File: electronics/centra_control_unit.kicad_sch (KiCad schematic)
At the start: 40 parts, among them J1 GND NetTie, J10 water_sensor_conn, J2 CAN, J3 Conn 12V Out 5ch, Q2 IRF6802SD, Q3 IRF6802SD, U1 AZ1117-ADJ, U10 BTS7006, U2 AZ1117-ADJ, U3 TJA1051T-3, U4 ESP32-S3-MINI-1U, U5 CD74HC4067SM, U6 BTS7006, U7 BTS7006, U8 BTS7006, U9 BTS7006

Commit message: porady od MichalaG
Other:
- added sheet water_sensors_logic (water_sensors_logic.kicad_sch)
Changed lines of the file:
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@@
 		)
 		(instances
-			(project ""
+			(project "electronics"
 				(path "/eeb1234c-eae0-4ac6-a30d-2a978d66d889/04c402f1-b99a-4823-99a0-0c7312782f29"
 					(reference "R1")
@@
 		)
 		(instances
-			(project ""
+			(project "electronics"
 				(path "/eeb1234c-eae0-4ac6-a30d-2a978d66d889/04c402f1-b99a-4823-99a0-0c7312782f29"
 					(reference "#PWR05")
@@
 		)
 		(instances
-			(project ""
+			(project "electronics"
 				(path "/eeb1234c-eae0-4ac6-a30d-2a978d66d889/04c402f1-b99a-4823-99a0-0c7312782f29"
 					(reference "Q2")
@@
 		)
 		(instances
-			(project ""
+			(project "electronics"
 				(path "/eeb1234c-eae0-4ac6-a30d-2a978d66d889/04c402f1-b99a-4823-99a0-0c7312782f29"
 					(reference "J1")
@@
 		)
 		(instances
-			(project ""
+			(project "electronics"
 				(path "/eeb1234c-eae0-4ac6-a30d-2a978d66d889/04c402f1-b99a-4823-99a0-0c7312782f29"
 					(reference "#PWR011")
@@
 		)
 		(instances
-			(project ""
+			(project "electronics"
 				(path "/eeb1234c-eae0-4ac6-a30d-2a978d66d889/04c402f1-b99a-4823-99a0-0c7312782f29"
 					(reference "#PWR018")
@@
 		)
 		(instances
-			(project ""
+			(project "electronics"
 				(path "/eeb1234c-eae0-4ac6-a30d-2a978d66d889/04c402f1-b99a-4823-99a0-0c7312782f29"
 					(reference "U3")
@@
 		)
 		(instances
-			(project ""
+			(project "electronics"
 				(path "/eeb1234c-eae0-4ac6-a30d-2a978d66d889/04c402f1-b99a-4823-99a0-0c7312782f29"
 					(reference "C2")
@@
 		)
 		(instances
-			(project ""
+			(project "electronics"
 				(path "/eeb1234c-eae0-4ac6-a30d-2a978d66d889/04c402f1-b99a-4823-99a0-0c7312782f29"
 					(reference "U4")
@@
 		)
 		(instances
-			(project ""
+			(project "electronics"
 				(path "/eeb1234c-eae0-4ac6-a30d-2a978d66d889/04c402f1-b99a-4823-99a0-0c7312782f29"
 					(reference "#PWR017")
@@
 		)
 		(instances
-			(project ""
+			(project "electronics"
 				(path "/eeb1234c-eae0-4ac6-a30d-2a978d66d889/04c402f1-b99a-4823-99a0-0c7312782f29"
 					(reference "U1")
@@
 		)
 		(instances
-			(project ""
+			(project "electronics"
 				(path "/eeb1234c-eae0-4ac6-a30d-2a978d66d889/04c402f1-b99a-4823-99a0-0c7312782f29"
 					(reference "Q2")
@@
 				)
 			)
+		)
+	)
+	(sheet
+		(at 151.13 19.05)
+		(size 21.59 13.97)
+		(fields_autoplaced yes)
+		(stroke
+			(width 0.1524)
+			(type solid)
+		)
+		(fill
+			(color 0 0 0 0.0000)
+		)
+		(property "Sheetname" "water_sensors_logic"
+			(at 151.13 18.3384 0)
+			(effects
+				(font
+					(size 1.27 1.27)
+				)
+				(justify left bottom)
+			)
+		)
+		(property "Sheetfile" "water_sensors_logic.kicad_sch"
+			(at 151.13 33.6046 0)
+			(effects
+				(font
+					(size 1.27 1.27)
+				)
+				(justify left top)
+			)
+		)
+		(instances
+			(project "electronics"
+				(path "/eeb1234c-eae0-4ac6-a30d-2a978d66d889/04c402f1-b99a-4823-99a0-0c7312782f29"
+					(page "6")
+				)
+			)

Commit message: lisbon flight changes
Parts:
- removed J10: water_sensor_conn, TerminalBlock:TerminalBlock_Xinya_XY308-2.54-6P_1x06_P2.54mm_Horizontal, symbol Connector_Generic:Conn_01x06
- removed J3: Conn 12V Out 5ch, TerminalBlock:TerminalBlock_bornier-5_P5.08mm, symbol Connector_Generic:Conn_01x05
- removed U5: CD74HC4067SM, Package_SO:SSOP-24_5.3x8.2mm_P0.65mm, symbol 74xx:CD74HC4067SM
- added J13: CH2, symbol Connector_Generic:Conn_01x01
- added J14: CH3, symbol Connector_Generic:Conn_01x01
- added J15: CH4, symbol Connector_Generic:Conn_01x01
- added J16: CH5, symbol Connector_Generic:Conn_01x01
- added J3: CH1, symbol Connector_Generic:Conn_01x01
- added U13: TMUX1108PW, Package_SO:TSSOP-16_4.4x5mm_P0.65mm, symbol Analog_Switch:TMUX1108PW
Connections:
- net +3.3V: now also U13.3 (VSS)
- net CH1_DIAG: now also U13.4 (S1)
- net CH2_DIAG: now also U13.5 (S2)
- net CH3_DIAG: now also U13.6 (S3)
- net CH4_DIAG: now also U13.7 (S4)
- net CH5_DIAG: now also U13.12 (S5)
- net HP_GND: no longer C_GND1.2, C_GND2.2, C_GND3.2, C_GND4.2, C_GND5.2, U10.1 (GND), U6.1 (GND), U7.1 (GND), U8.1 (GND), U9.1 (GND)
- net MUX_ANALOG_COM: now also U13.8 (D)
- net MUX_S0: now also U13.1 (A0)
- net MUX_S1: now also U13.16 (A1)
- net MUX_S2: now also U13.15 (A2)
- net at C_GND1.1, U6.10 (OUT), U6.12 (OUT)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: now also J3.1 (Pin_1)
- net at C_GND2.1, U7.10 (OUT), U7.12 (OUT)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: now also J13.1 (Pin_1)
- net at C_GND3.1, U8.10 (OUT), U8.12 (OUT)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: now also J14.1 (Pin_1)
- net at C_GND4.1, U9.10 (OUT), U9.12 (OUT)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: now also J15.1 (Pin_1)
- net at C_GND5.1, U10.10 (OUT), U10.12 (OUT)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: now also J16.1 (Pin_1)
- new net GND_HP: C_GND1.2, C_GND2.2, C_GND3.2, C_GND4.2, C_GND5.2, U10.1 (GND), U6.1 (GND), U7.1 (GND), U8.1 (GND), U9.1 (GND)
- new net GND_LP: U13.14 (GND)
- no-connect marks 19 -> 13

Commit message: flight back. different layout. start analog ui
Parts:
- removed C1, C2: 10uF, Capacitor_SMD:C_0805_2012Metric_Pad1.18x1.45mm_HandSolder, symbol Device:C
- removed C3, C4: 22uF, Capacitor_SMD:C_0805_2012Metric_Pad1.18x1.45mm_HandSolder, symbol Device:C
- removed C_GND1, C_GND2, C_GND3, C_GND4, C_GND5: 10nF, Capacitor_SMD:C_0805_2012Metric_Pad1.18x1.45mm_HandSolder, symbol Device:C_Small
- removed J1: GND NetTie, Connector_PinHeader_1.00mm:PinHeader_1x02_P1.00mm_Vertical, symbol Connector_Generic:Conn_01x02
- removed J13: CH2, symbol Connector_Generic:Conn_01x01
- removed J14: CH3, symbol Connector_Generic:Conn_01x01
- removed J15: CH4, symbol Connector_Generic:Conn_01x01
- removed J16: CH5, symbol Connector_Generic:Conn_01x01
- removed J2: CAN, TerminalBlock:TerminalBlock_Xinya_XY308-2.54-2P_1x02_P2.54mm_Horizontal, symbol Connector_Generic:Conn_01x02
- removed J3: CH1, symbol Connector_Generic:Conn_01x01
- removed Q2, Q3: IRF6802SD, Package_DirectFET:DirectFET_SA, symbol Transistor_FET:IRF6802SD
- removed R1, R3: 125, Resistor_SMD:R_0805_2012Metric_Pad1.20x1.40mm_HandSolder, symbol Device:R
- removed R2: 205, Resistor_SMD:R_0805_2012Metric_Pad1.20x1.40mm_HandSolder, symbol Device:R
- removed R4: 370, Resistor_SMD:R_0805_2012Metric_Pad1.20x1.40mm_HandSolder, symbol Device:R
- removed R_DEN1, R_DEN2, R_DEN3, R_DEN4, R_DEN5, R_IN1, R_IN2, R_IN3, R_IN4, R_IN5: 4.7k, Resistor_SMD:R_0805_2012Metric_Pad1.20x1.40mm_HandSolder, symbol Device:R
- removed U1, U2: AZ1117-ADJ, Package_TO_SOT_SMD:SOT-223-3_TabPin2, symbol Regulator_Linear:AZ1117-ADJ
- removed U10, U6, U7, U8, U9: BTS7006, Package_SO:Infineon_PG-TSDSO-14-22, symbol Power_Management:BTS7004-1EPP
- removed U13: TMUX1108PW, Package_SO:TSSOP-16_4.4x5mm_P0.65mm, symbol Analog_Switch:TMUX1108PW
- removed U3: TJA1051T-3, Package_SO:SOIC-8_3.9x4.9mm_P1.27mm, symbol Interface_CAN_LIN:TJA1051T-3
- added FB2: FerriteBead 47 Ohm, Inductor_SMD:L_Walsin_WLFM201609x, symbol Device:FerriteBead
- added U14: CD74HC4067SM, Package_SO:SSOP-24_5.3x8.2mm_P0.65mm, symbol 74xx:CD74HC4067SM
- added U15: TCA9555PWR, Package_SO:TSSOP-24_4.4x7.8mm_P0.65mm, symbol Interface_Expansion:TCA9555PWR
- added U18: SN74LV4051A, symbol 74xx:74LS151
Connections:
- net GND is gone; now on net GND_LP: U4.1 (GND), U4.2 (GND), U4.42 (GND), U4.43 (GND), U4.46 (GND), U4.47 (GND), U4.48 (GND), U4.49 (GND), U4.50 (GND), U4.51 (GND), U4.52 (GND), U4.53 (GND), U4.54 (GND), U4.55 (GND), U4.56 (GND), U4.57 (GND), U4.58 (GND), U4.59 (GND), U4.60 (GND), U4.61 (GND), U4.62 (GND), U4.63 (GND), U4.64 (GND), U4.65 (GND)
- net GND_HP: now also FB2.2
- net GND_LP: now also FB2.1, U15.12 (GND), U15.2 (A1), U15.21 (A0), U15.3 (A2)
- net SCL: now also U15.22 (SCL)
- net SDA: now also U15.23 (SDA)
- net CAN_RX: no longer names the net of U4.13 (IO9)
- net CAN_SLEEP: no longer names the net of U4.14 (IO10)
- net CAN_TX: no longer names the net of U4.12 (IO8)
- net CH1_DIAG_EN renamed ch4_diag
- net CH1_IN renamed ch5_diag
- net CH2_DAIG_EN renamed ch2_diag
- net CH2_IN renamed ch3_diag
- net CH3_DAIG_EN: no longer names the net of U4.35 (IO39)
- net CH3_DAIG_EN: now also U15.1 (~{INT})
- net CH3_IN renamed ch1_diag
- net CH4_DAIG_EN: no longer names the net of U4.33 (IO37)
- net CH4_IN: no longer names the net of U4.34 (IO38)
- net CH5_DAIG_EN: no longer names the net of U4.31 (IO35)
- net CH5_IN: no longer names the net of U4.32 (IO36)
- net MUX_ANALOG_COM renamed 230VAC/AC_DETECT
- net MUX_S0 renamed temp_sensors/1-WIRE
- net MUX_S1 renamed CAN/CAN_SLEEP
- net MUX_S2 renamed CAN/CAN_RX
- net MUX_S3 renamed CAN/CAN_TX
- net water_sens_enable renamed 230VAC/RELAY_IN
- new net digital_switching/CH1_DEN: U15.11 (P07)
- new net digital_switching/CH1_IN: U15.10 (P06)
- new net digital_switching/CH2_DEN: U15.14 (P11)
- new net digital_switching/CH2_IN: U15.13 (P10)
- new net digital_switching/CH3_DEN: U15.16 (P13)
- new net digital_switching/CH3_IN: U15.15 (P12)
- new net digital_switching/CH4_DEN: U15.18 (P15)
- new net digital_switching/CH4_IN: U15.17 (P14)
- new net digital_switching/CH5_DEN: U15.20 (P17)
- new net digital_switching/CH5_IN: U15.19 (P16)
- new net water_sensors_logic/GREY_WATER_FULL: U15.9 (P05)
- new net water_sensors_logic/WS_ENABLE: U15.4 (P00)
- new net water_sensors_logic/WS_LVL_100%: U15.8 (P04)
- new net water_sensors_logic/WS_LVL_25%: U15.5 (P01)
- new net water_sensors_logic/WS_LVL_50%: U15.6 (P02)
- new net water_sensors_logic/WS_LVL_75%: U15.7 (P03)
- no-connect marks 13 -> 23
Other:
- added sheet 230VAC (230VAC.kicad_sch)
- added sheet CAN (CAN.kicad_sch)
- added sheet dc_dc_conversion (dc_dc_conversion.kicad_sch)
- added sheet digital_switching (digital_switching.kicad_sch)
- added sheet rgb_led_control (rgb_led_control.kicad_sch)
- added sheet temp_sensors (temp_sensors.kicad_sch)
- sheet water_sensors_logic ports: added GREY_WATER_FULL, WS_ENABLE, WS_LVL_100%, WS_LVL_25%, WS_LVL_50%, WS_LVL_75%; removed none
- note removed: "LED controls"
- note removed: "Vout=Vref*(1+R2/R1) + Iadj*R2"
- moved on the sheet: D1

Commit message: no tracks, but placement looks good
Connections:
- net +3.3V: now also U15.24 (VCC)
- net +BATT renamed V_Bat
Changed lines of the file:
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@@
 	)
 	(no_connect
-		(at 111.76 53.34)
+		(at 115.57 53.34)
 	)
 	(no_connect
@@
 	(wire
 		(pts
-			(xy 113.03 53.34) (xy 115.57 53.34)
-		)
-		(stroke
-			(width 0)
-			(type default)
-		)
-	)
-	(wire
-		(pts
 			(xy 218.44 62.23) (xy 236.22 62.23)
 		)
@@
 		)
 	)
-	(label "V_Bat"
-		(at 30.48 21.59 0)
-		(fields_autoplaced yes)
-		(effects
-			(font
-				(size 1.27 1.27)
-			)
-			(justify left bottom)
-		)
-	)
 	(label "SCL"
 		(at 109.22 71.12 0)
@@
 	)
 	(label "strap pin"
-		(at 113.03 53.34 180)
+		(at 115.57 53.34 180)
 		(fields_autoplaced yes)
 		(effects
@@
 			)
 			(justify left bottom)
+		)
+	)
+	(global_label "V_Bat"
+		(shape passive)
+		(at 26.67 21.59 180)
+		(fields_autoplaced yes)
+		(effects
+			(font
+				(size 1.27 1.27)
+			)
+			(justify right)
+		)
+		(property "Intersheetrefs" "${INTERSHEET_REFS}"
+			(at 19.5952 21.59 0)
+			(effects
+				(font
+					(size 1.27 1.27)
+				)
+				(justify right)
+				(hide yes)
+			)
 		)
 	)
@@
 		(shape passive)
 		(at 107.95 68.58 180)
-		(fields_autoplaced yes)
-		(effects
-			(font
-				(size 1.27 1.27)
-			)
-			(justify right)
-		)
-	)
-	(hierarchical_label "+BATT"
-		(shape input)
-		(at 26.67 21.59 180)
 		(fields_autoplaced yes)
 		(effects
@@
 					(unit 1)
 				)
+			)
+		)
+	)
+	(symbol
+		(lib_id "power:+3.3V")
+		(at 200.66 41.91 0)
+		(unit 1)
+		(exclude_from_sim no)
+		(in_bom yes)
+		(on_board yes)
+		(dnp no)
+		(fields_autoplaced yes)
+		(property "Reference" "#PWR08"
+			(at 200.66 45.72 0)
+			(effects
+				(font
+					(size 1.27 1.27)
+				)
+				(hide yes)
+			)
+		)
+		(property "Value" "+3.3V"
+			(at 200.66 36.83 0)
+			(effects
+				(font
+					(size 1.27 1.27)
+				)
+			)
+		)
+		(property "Footprint" ""
+			(at 200.66 41.91 0)
+			(effects
+				(font
+					(size 1.27 1.27)
+				)
+				(hide yes)
+			)
+		)
+		(property "Datasheet" ""
+			(at 200.66 41.91 0)
+			(effects
+				(font
+					(size 1.27 1.27)
+				)
+				(hide yes)
+			)
+		)
+		(property "Description" "Power symbol creates a global label with name \"+3.3V\""
+			(at 200.66 41.91 0)
+			(effects
+				(font
+					(size 1.27 1.27)
+				)
+				(hide yes)
+			)
+		)
+		(pin "1"
+		)
+		(instances
+			(project "electronics"
+				(path "/eeb1234c-eae0-4ac6-a30d-2a978d66d889/04c402f1-b99a-4823-99a0-0c7312782f29"
+					(reference "#PWR08")
+					(unit 1)
+				)

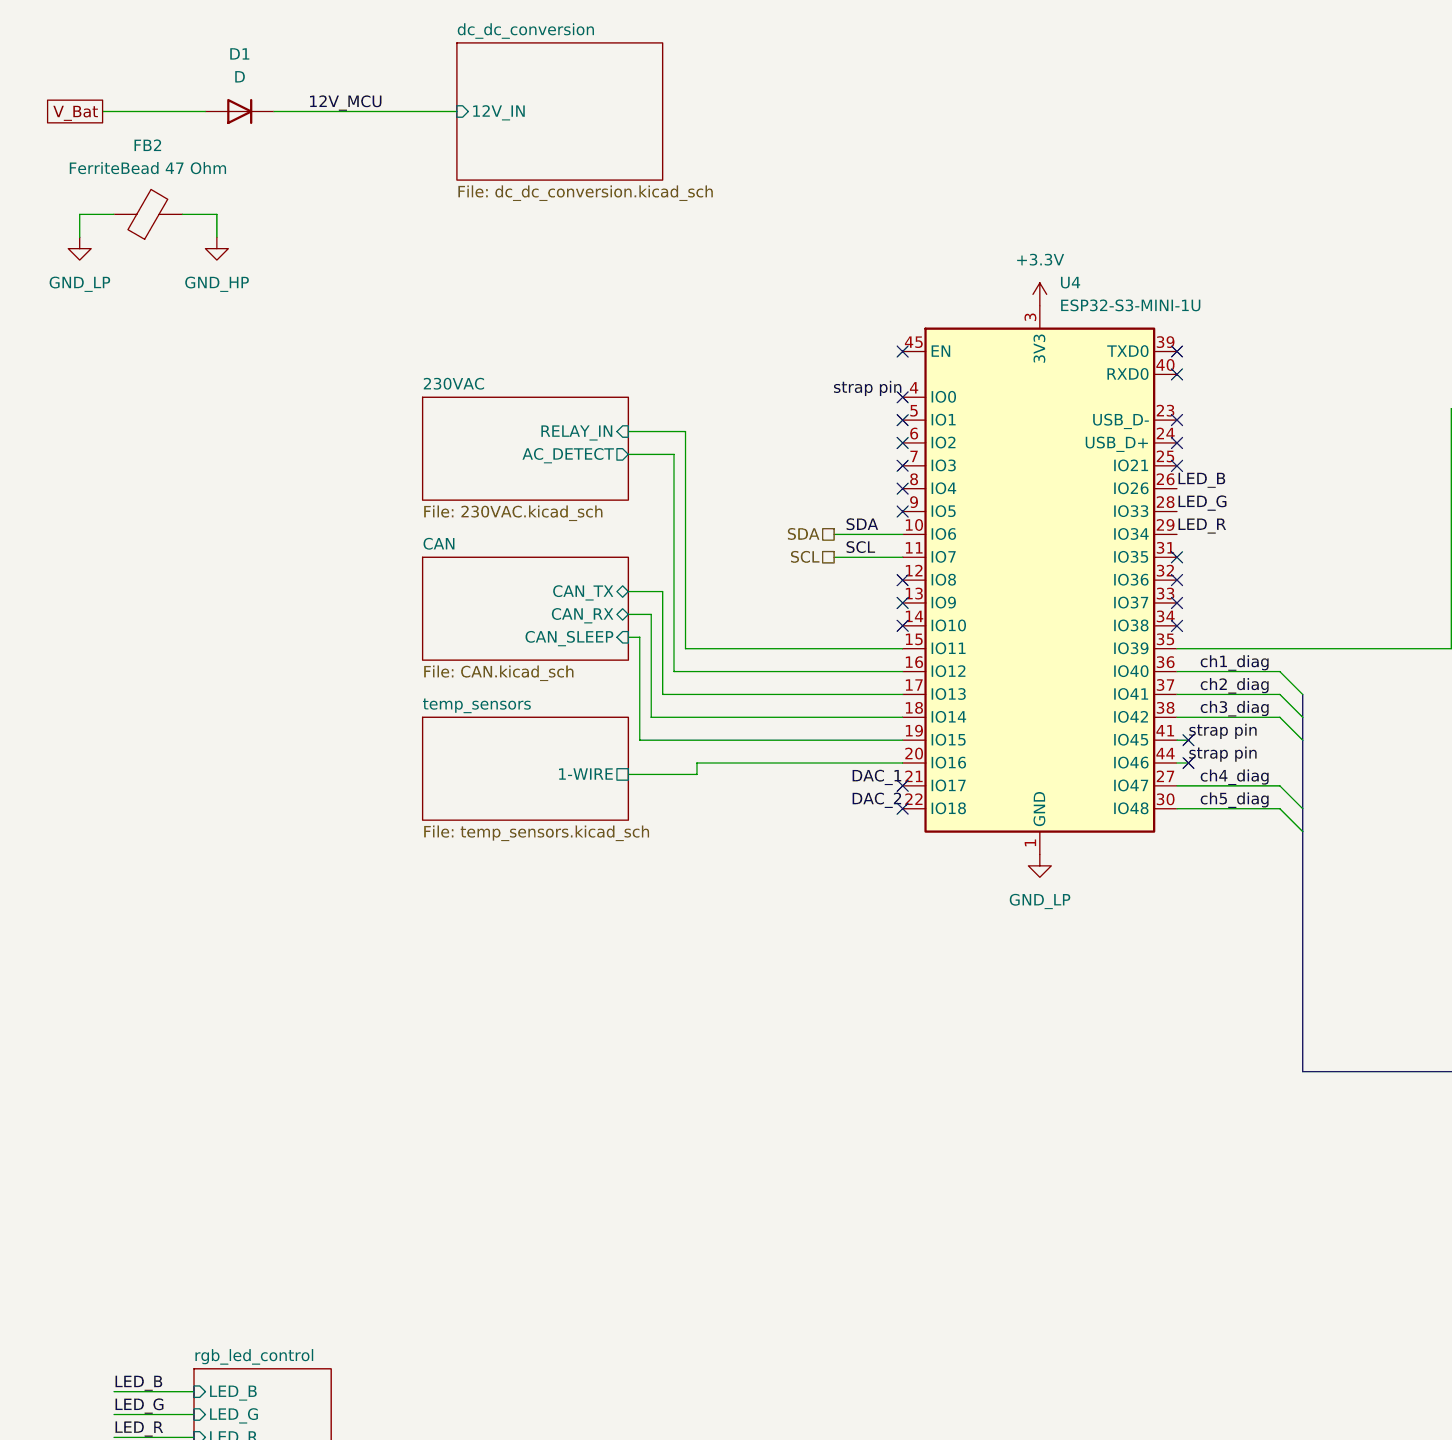
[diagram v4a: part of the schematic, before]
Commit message: add some more part nummbers
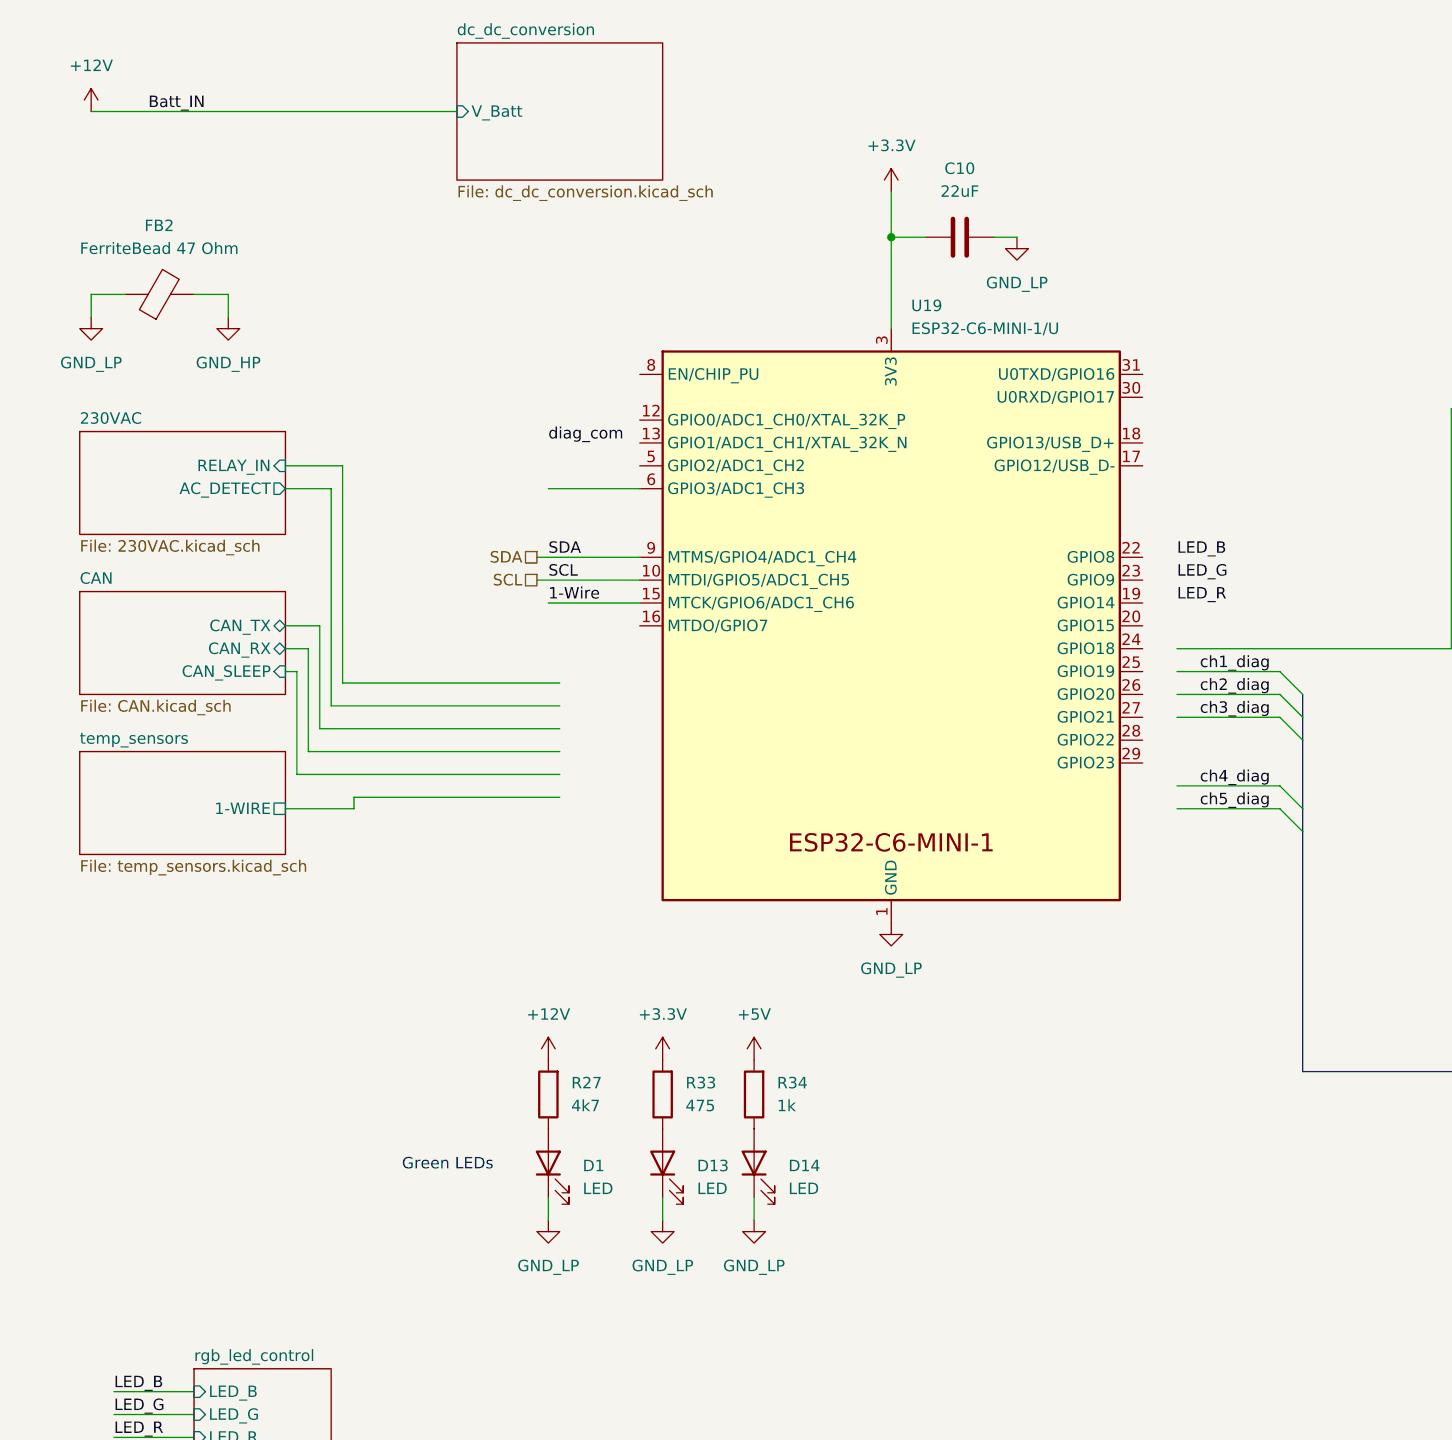
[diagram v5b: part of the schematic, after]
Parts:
- removed D1: D, Diode_SMD:D_1210_3225Metric_Pad1.42x2.65mm_HandSolder, symbol Device:D
- removed U4: ESP32-S3-MINI-1U, RF_Module:ESP32-S2-MINI-1U, symbol RF_Module:ESP32-S3-MINI-1U
- added C10: 22uF, Capacitor_SMD:C_0805_2012Metric_Pad1.18x1.45mm_HandSolder, symbol Device:C
- added D1, D13, D14: LED, symbol Device:LED
- added R27: 4k7, Resistor_SMD:R_0805_2012Metric_Pad1.20x1.40mm_HandSolder, symbol Device:R
- added R33: 475, Resistor_SMD:R_0805_2012Metric_Pad1.20x1.40mm_HandSolder, symbol Device:R
- added R34: 1k, Resistor_SMD:R_0805_2012Metric_Pad1.20x1.40mm_HandSolder, symbol Device:R
- added U19: ESP32-C6-MINI-1/U, PCM_Espressif:ESP32-C6-MINI-1, symbol Espressif:ESP32-C6-MINI-1/U
- U15: LCSC (none) -> C465732; TME (none) -> TCA9554APWR
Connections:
- net +3.3V: now also C10.2, R33.2, U19.3 (3V3)
- net GND_LP: now also C10.1, D1.1 (K), D13.1 (K), D14.1 (K), U19.1 (GND), U19.11 (GND), U19.14 (GND), U19.2 (GND), U19.36 (GND), U19.37 (GND), U19.38 (GND), U19.39 (GND), U19.40 (GND), U19.41 (GND), U19.42 (GND), U19.43 (GND), U19.44 (GND), U19.45 (GND), U19.46 (GND), U19.47 (GND), U19.48 (GND), U19.49 (GND), U19.50 (GND), U19.51 (GND), U19.52 (GND), U19.53 (GND)
- net SCL: now also U19.10 (MTDI/GPIO5/ADC1_CH5)
- net SDA: now also U19.9 (MTMS/GPIO4/ADC1_CH4)
- new net: D13.2 (A), R33.1
- new net: D1.2 (A), R27.1
- new net: D14.2 (A), R34.1
- new net +12V: R27.2
- new net +5V: R34.2
- new net 1-Wire: U19.15 (MTCK/GPIO6/ADC1_CH6)
- no-connect marks 23 -> 0
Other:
- sheet dc_dc_conversion ports: added V_Batt; removed 12V_IN
- note added: "Green LEDs"
- moved on the sheet: FB2
